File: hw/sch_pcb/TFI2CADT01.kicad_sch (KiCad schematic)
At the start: 38 parts, among them J1 SM04B-GHS-TB, J2 SM04B-GHS-TB, J3 SM04B-GHS-TB, J4 SM04B-GHS-TB, J5 SM04B-GHS-TB, J6 SM04B-GHS-TB, M1 HOLE, M2 HOLE, M3 HOLE, M4 HOLE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

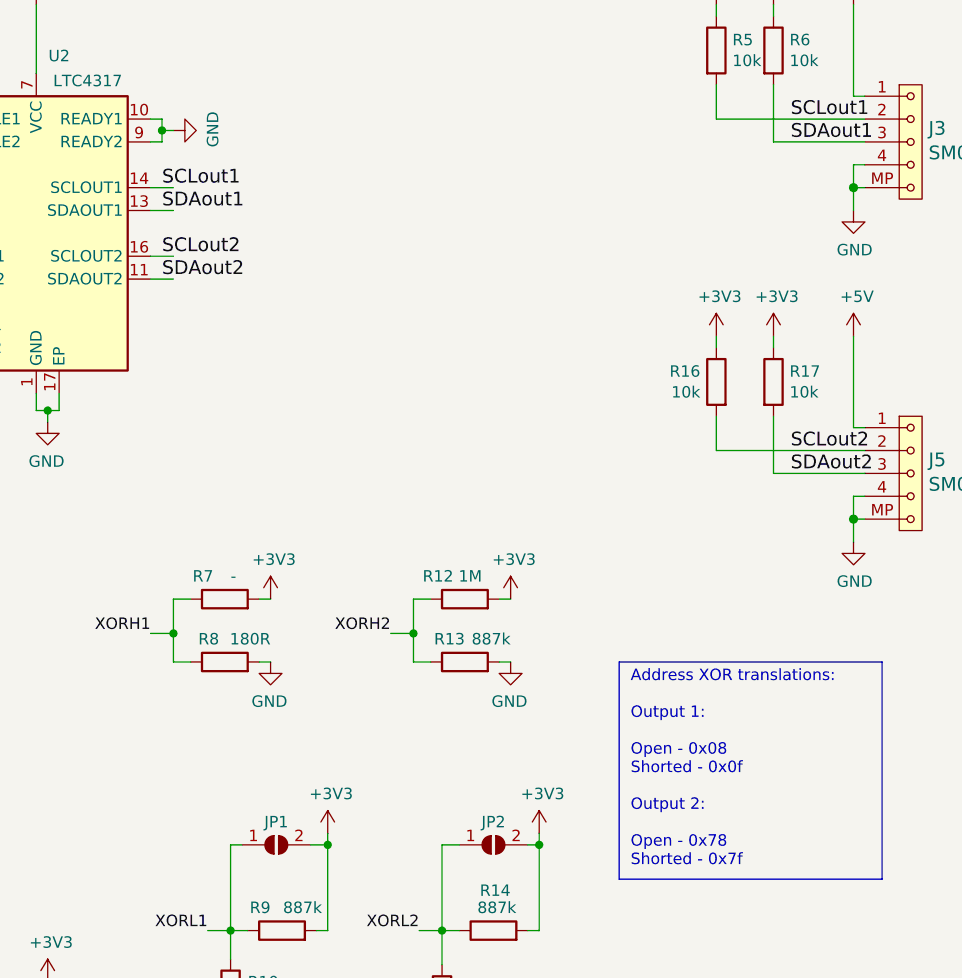
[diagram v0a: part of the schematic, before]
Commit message: Improve schematics layout.
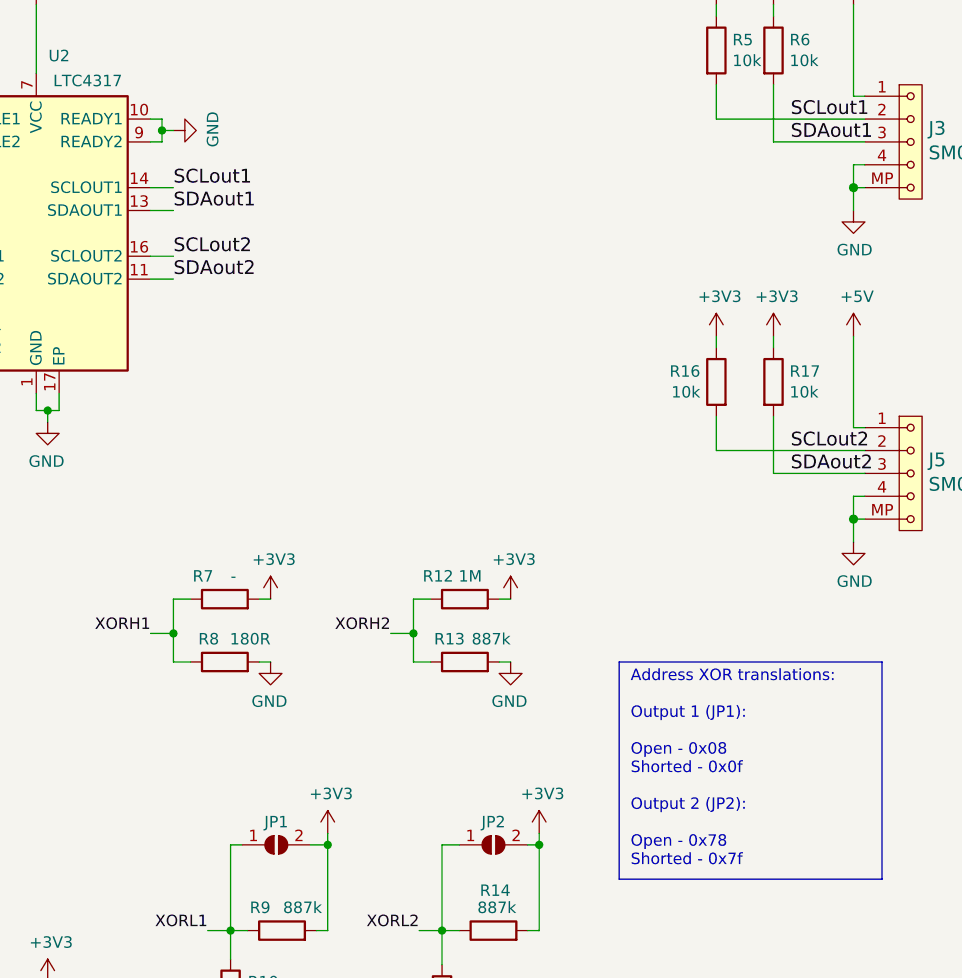
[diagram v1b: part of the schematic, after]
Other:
- note added: "Address XOR translations: Output 1 (JP1): Open - 0x08 Shorted - 0x0f Output 2 (JP2): Open - 0x78 Shorted - 0x7f"
- note removed: "Address XOR translations: Output 1: Open - 0x08 Shorted - 0x0f Output 2: Open - 0x78 Shorted - 0x7f"
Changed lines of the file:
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@@
     (stroke (width 0) (type solid))
   )
-  (text "Address XOR translations:\n\nOutput 1:\n\nOpen - 0x08\nShorted - 0x0f\n\nOutput 2:\n\nOpen - 0x78\nShorted - 0x7f"
+  (text "Address XOR translations:\n\nOutput 1 (JP1):\n\nOpen - 0x08\nShorted - 0x0f\n\nOutput 2 (JP2):\n\nOpen - 0x78\nShorted - 0x7f"
     (at 175.26 156.21 0)
     (effects (font (size 1.27 1.27)) (justify left bottom))
@@
     (effects (font (size 1.27 1.27)) (justify right bottom))
   )
-  (label "SDAout1" (at 123.19 83.185 0) (fields_autoplaced)
+  (label "SDAout1" (at 124.46 83.185 0) (fields_autoplaced)
     (effects (font (size 1.524 1.524)) (justify left bottom))
   )
@@
     (effects (font (size 1.524 1.524)) (justify right bottom))
   )
-  (label "SDAout2" (at 123.19 90.805 0) (fields_autoplaced)
+  (label "SDAout2" (at 124.46 90.805 0) (fields_autoplaced)
     (effects (font (size 1.524 1.524)) (justify left bottom))
   )
@@
     (effects (font (size 1.524 1.524)) (justify right bottom))
   )
-  (label "SCLout1" (at 123.19 80.645 0) (fields_autoplaced)
+  (label "SCLout1" (at 124.46 80.645 0) (fields_autoplaced)
     (effects (font (size 1.524 1.524)) (justify left bottom))
   )
-  (label "SCLout2" (at 123.19 88.265 0) (fields_autoplaced)
+  (label "SCLout2" (at 124.46 88.265 0) (fields_autoplaced)
     (effects (font (size 1.524 1.524)) (justify left bottom))
   )

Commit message: Update project to KiCADv9.
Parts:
- G1: symbol MLAB_TF_LOGO:LOGO -> TF_LOGO:LOGO
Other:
- title: TFI2CEXT01A -> TFI2CADT01B
